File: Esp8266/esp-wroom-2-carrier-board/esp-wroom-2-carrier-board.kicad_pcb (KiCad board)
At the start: 2 copper layers, 28 parts, among them J1 DF9B-19S-1V69, J2 USB_B_Mini, Q1 MMBT2222A, Q2 MMBT2222A, U1 ESP-WROOM-02, U2 FT231XQ, U3 TPS5410DR

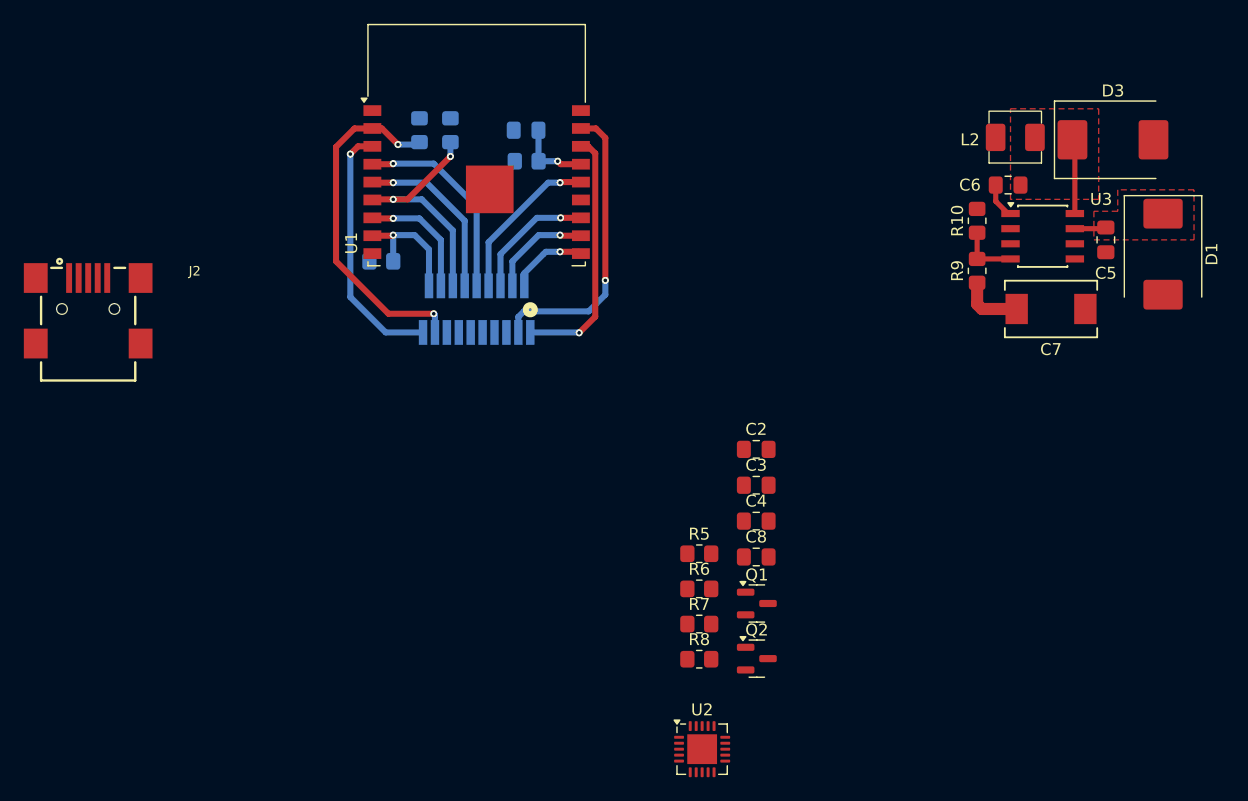
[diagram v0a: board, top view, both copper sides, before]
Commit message: Board Layout
Changed board layout to something smaller
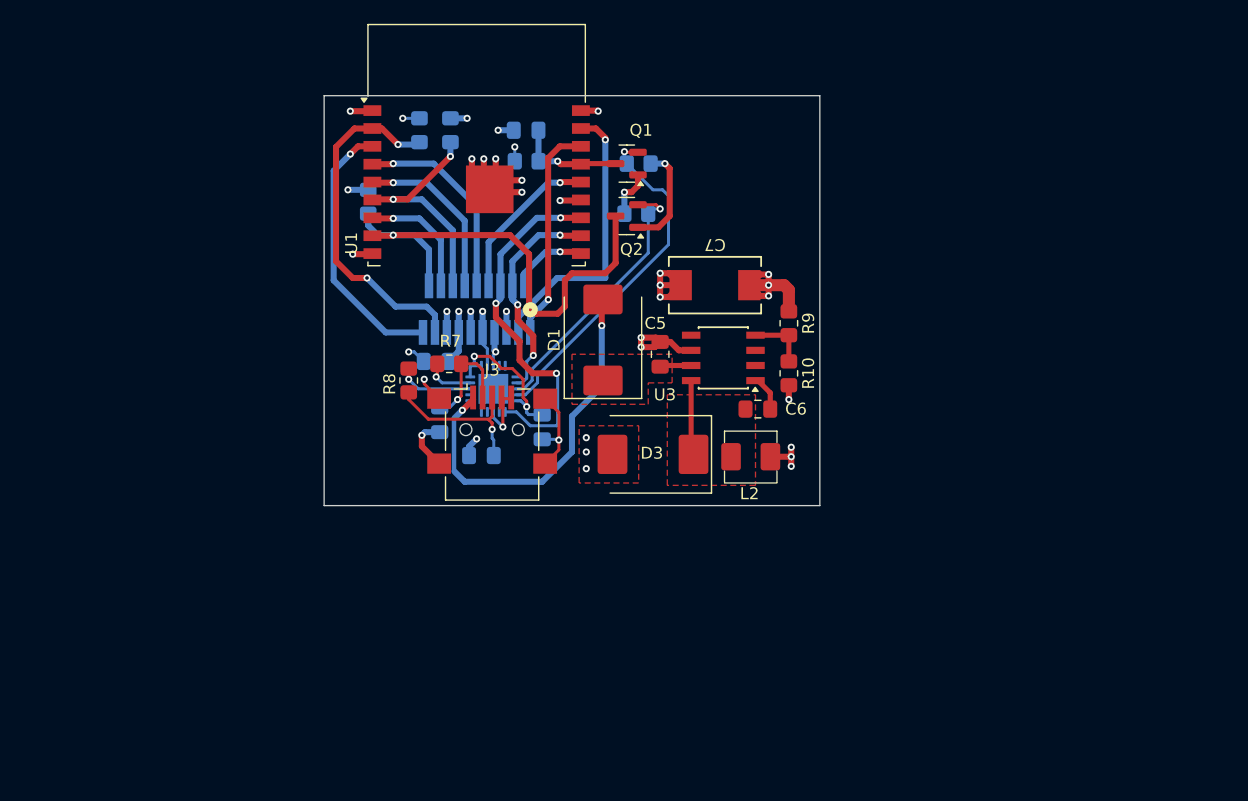
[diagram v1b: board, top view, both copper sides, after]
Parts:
- removed J2: USB_B_Mini, User_Footprint:Usb_B_mini_Wurth_65100516121
- added J3: USB_B_Mini, Connector_USB:USB_Mini-B_Lumberg_2486_01_Horizontal, F.Cu at (133.9, 101.7)
- C2, C3, C4, C8, R5, R6, U2: moved to B.Cu
- moved D1 47.5 mm to (143.2, 94.2), turned to 90 degrees
- moved D3 46.8 mm to (147.4, 103.8), turned to 180 degrees
- moved Q2 38.7 mm to (145.2, 83.8), turned to 180 degrees
- moved C5 38.6 mm to (148.0, 95.4), turned to -90 degrees
- moved Q1 38.5 mm to (145.2, 79.4), turned to 180 degrees
- moved R6 36.1 mm to (146.2, 79.4)
- moved U2 34.9 mm to (134.0, 98.3), turned to 90 degrees
- moved L2 34.8 mm to (155.6, 104.0), turned to 0 degrees
- moved R8 33.8 mm to (126.9, 97.6), turned to -90 degrees
- moved C8 31.5 mm to (129.2, 96.0), turned to 180 degrees
- moved R7 30.3 mm to (130.3, 96.2)
- moved R5 29.0 mm to (146.0, 83.6), turned to 180 degrees
- moved U3 28.7 mm to (153.3, 95.7), turned to 180 degrees
- moved C7 28.3 mm to (152.6, 89.6), turned to 180 degrees
- moved C6 28.2 mm to (156.2, 100.0), turned to 180 degrees
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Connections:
- J1 pad 11: unconnected-(J1-Pad11) -> GND
- J1 pad 13: /Microcontroller/IO13 -> +3.3V
- J1 pad 15: unconnected-(J1-Pad15) -> GND
- J1 pad 5: unconnected-(J1-Pad5) -> +3.3V
- J1 pad 7: unconnected-(J1-Pad7) -> GND
- J1 pad 9: unconnected-(J1-Pad9) -> +3.3V
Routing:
- net GND: track 0.00 -> 69.5 mm, vias 0 -> 28
- net /Microcontroller/IO0: track 10.5 -> 42.7 mm
- net /Microcontroller/Vbus: track 0.00 -> 31.9 mm, vias 0 -> 2
- net /Microcontroller/~{RTS}: track 0.00 -> 29.3 mm, vias 0 -> 1
- net +3.3V: track 5.28 -> 31.6 mm, vias 0 -> 13
- net /Microcontroller/~{DTR}: track 0.00 -> 22.8 mm, vias 0 -> 1
- net /Microcontroller/TX0: track 10.7 -> 30.8 mm, vias 1 -> 3
- net /Microcontroller/D+: track 0.00 -> 13.1 mm, vias 0 -> 1
- net Net-(U2-3V3OUT): track 0.00 -> 13.0 mm, vias 0 -> 2
- net /Microcontroller/RX0: track 8.74 -> 18.5 mm, vias 1 -> 3
- net /Microcontroller/D-: track 0.00 -> 9.33 mm, vias 0 -> 1
- net Net-(Q2-B): track 0.00 -> 8.82 mm, vias 0 -> 1
- net Net-(U2-USBDP): track 0.00 -> 6.39 mm, vias 0 -> 1
- net Net-(U2-USBDM): track 0.00 -> 4.21 mm, vias 0 -> 1
- net Net-(Q1-B): track 0.00 -> 4.07 mm, vias 0 -> 1
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- added copper zone on In2.Cu, net +3.3V
- added copper zone on F.Cu, net GND
- added copper zone on In1.Cu, net GND
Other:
- board outline added: 41.6 x 34.4 mm
- copper layers 2 -> 4

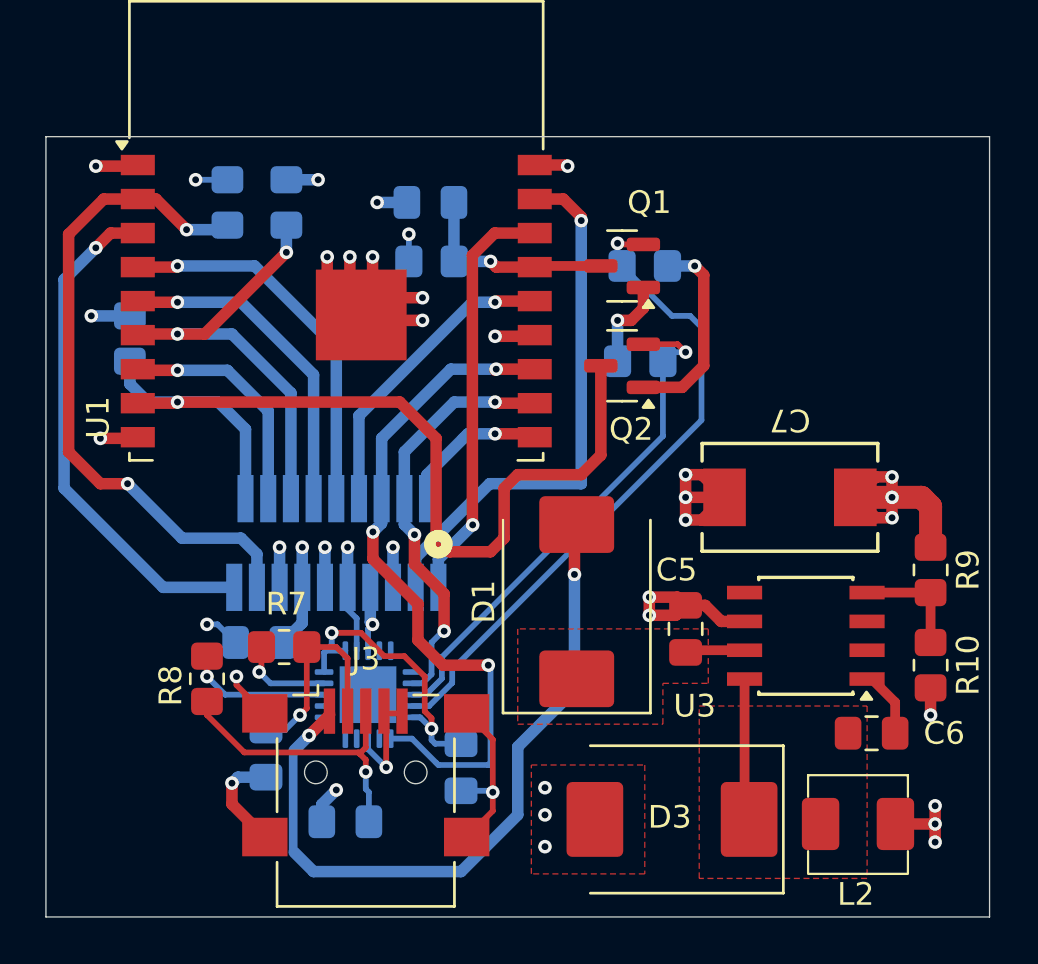
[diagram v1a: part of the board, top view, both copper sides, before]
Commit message: capacitor layout
Changed capacitor position to front layer to have enough clearance on bottom layer
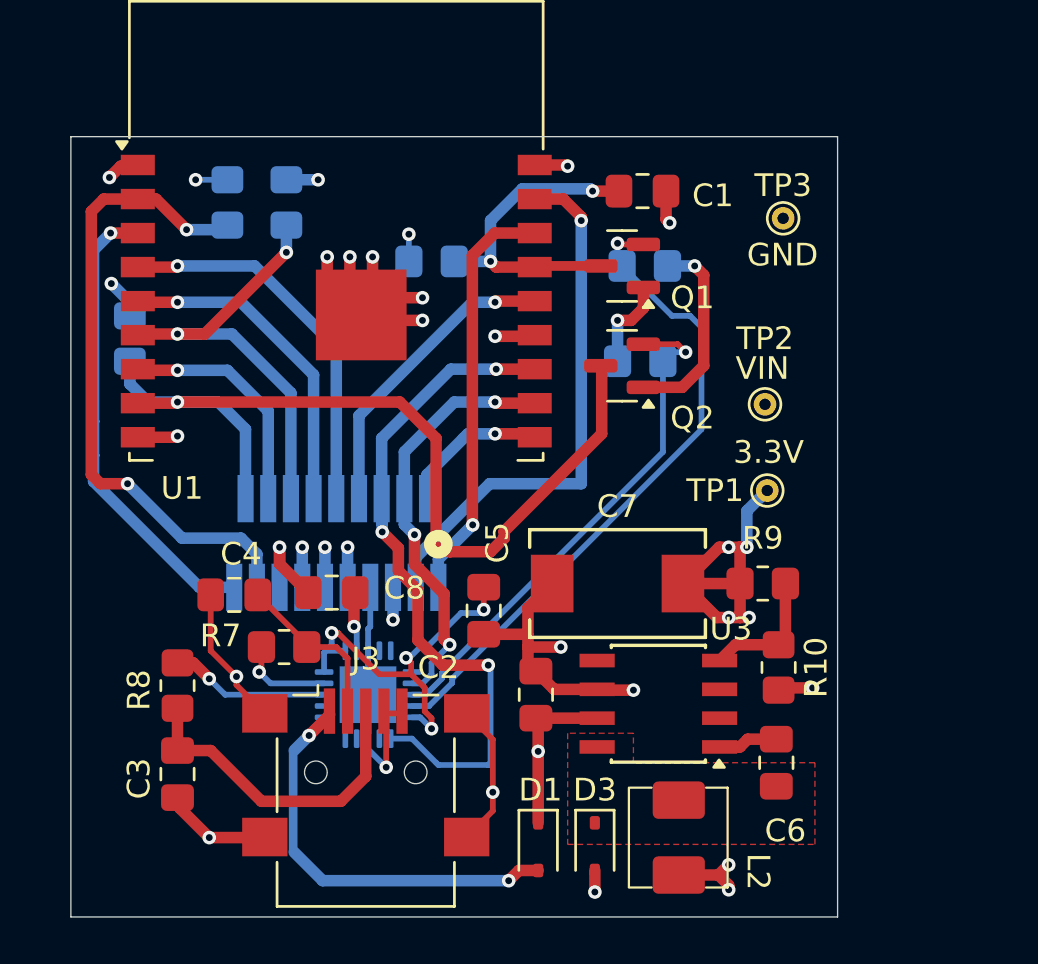
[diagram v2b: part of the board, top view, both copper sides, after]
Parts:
- added TP1: 3.3V, TestPoint:TestPoint_THTPad_D1.0mm_Drill0.5mm, F.Cu at (151.6, 89.3)
- added TP2: VIN, TestPoint:TestPoint_THTPad_D1.0mm_Drill0.5mm, F.Cu at (151.5, 85.5)
- added TP3: GND, TestPoint:TestPoint_THTPad_D1.0mm_Drill0.5mm, F.Cu at (152.3, 77.3)
- C1, C2, C3, C4, C8: moved to F.Cu
- D1: value B340 -> 1N5819ws; footprint Diode_SMD:D_SMC -> Diode_SMD:D_SOD-323
- D3: value B340 -> 1N5819WS; footprint Diode_SMD:D_SMC -> Diode_SMD:D_SOD-323
- moved D1 10.9 mm to (141.5, 105.0), turned to -90 degrees
- moved C1 9.36 mm to (146.1, 76.1), turned to 0 degrees
- moved C7 8.50 mm to (145.0, 93.4)
- moved L2 7.92 mm to (147.7, 104.6), turned to -90 degrees
- moved C3 7.69 mm to (125.6, 101.8), turned to -90 degrees
- moved R9 7.42 mm to (151.4, 93.4), turned to 0 degrees
- moved C5 7.21 mm to (141.4, 98.3)
- moved U3 7.16 mm to (146.8, 98.7)
- moved C4 7.14 mm to (128.1, 93.9), turned to 180 degrees
- moved C2 6.97 mm to (139.1, 94.6)
- moved R10 6.70 mm to (152.1, 97.1)
- moved C6 4.40 mm to (152.0, 101.3), turned to -90 degrees
- moved C8 3.88 mm to (132.4, 93.8)
- moved D3 3.61 mm to (144.0, 105.0), turned to -90 degrees
- moved R8 1.33 mm to (125.6, 97.9)
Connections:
- J1 pad 5: +3.3V -> /Microcontroller/VIN
- J1 pad 9: +3.3V -> /Microcontroller/VIN
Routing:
- net /Microcontroller/VIN: track 2.64 -> 45.3 mm, vias 0 -> 3
- net /Microcontroller/Vbus: track 31.9 -> 18.3 mm
- net /Power/PH: track 6.27 -> 0.00 mm
- net /Microcontroller/Reset: track 9.19 -> 14.7 mm, vias 1 -> 2
- net Net-(U2-3V3OUT): track 13.0 -> 16.9 mm, vias 2 -> 4
- net GND: track 69.5 -> 72.4 mm, vias 28 -> 20
- net +3.3V: track 31.6 -> 28.9 mm, vias 13 -> 12
- net /Microcontroller/IO14: track 22.6 -> 20.6 mm
- net /Microcontroller/D-: track 9.33 -> 7.63 mm, vias 1 -> 0
- net /Microcontroller/IO0: track 42.7 -> 41.1 mm
- net /Microcontroller/D+: track 13.1 -> 14.5 mm, vias 1 -> 0
- net /Microcontroller/EN: track 29.5 -> 28.7 mm
- net Net-(U3-VSENSE): track 5.00 -> 5.71 mm
- net Net-(U2-USBDP): track 6.39 -> 7.04 mm
- removed copper zone on F.Cu, net /Microcontroller/VIN
- removed copper zone on F.Cu, net GND
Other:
- board size 41.6 x 34.4 mm -> 33.8 x 34.4 mm
- board text added: "3.3V"
- board text added: "GND"
- board text added: "VIN"

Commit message: Traces
Layout traces for the PCB
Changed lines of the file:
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@@
 			(at -2.3 0 0)
 			(layer "F.SilkS")
+			(hide yes)
 			(effects
 				(font
@@
 			(size 1 1)
 			(drill 0.5)
-			(layers "F&B.Cu" "*.Mask")
+			(layers "*.Cu" "*.Mask")
 			(remove_unused_layers no)
 			(net 8 "+3.3V")
@@
 		(tags "resistor handsolder")
 		(property "Reference" "R10"
-			(at 0 -1.65 90)
+			(at -1.1 -1.65 90)
 			(layer "F.SilkS")
 			(effects
@@
 		(tags "resistor handsolder")
 		(property "Reference" "R9"
-			(at 0 -2 0)
+			(at 1.1 -1.9 0)
 			(layer "F.SilkS")
 			(effects
@@
 			(at 0 -2.9 0)
 			(layer "F.SilkS")
+			(hide yes)
 			(effects
 				(font
@@
 			(at 0 -1.448 0)
 			(layer "F.SilkS")
+			(hide yes)
 			(effects
 				(font
@@
 	)
 	(gr_text "GND"
-		(at 150.7 79.5 0)
+		(at 150.7 76 0)
 		(layer "F.SilkS")
 		(effects
@@
 		)
 	)
+	(dimension
+		(type orthogonal)
+		(layer "User.1")
+		(pts
+			(xy 132.599999 91.6) (xy 121 91.5)
+		)
+		(height -32.1)
+		(orientation 0)
+		(format
+			(prefix "")
+			(suffix "")
+			(units 3)
+			(units_format 0)
+			(precision 4)
+			(suppress_zeroes yes)
+		)
+		(style
+			(thickness 0.1)
+			(arrow_length 1.27)
+			(text_position_mode 0)
+			(arrow_direction outward)
+			(extension_height 0.58642)
+			(extension_offset 0.5)
+			(keep_text_aligned yes)
+		)
+		(gr_text "11.6"
+			(at 126.799999 58.35 0)
+			(layer "User.1")
+			(effects
+				(font
+					(size 1 1)
+					(thickness 0.15)
+				)
+			)
+		)
+	)
+	(dimension
+		(type orthogonal)
+		(layer "User.1")
+		(pts
+			(xy 132.599999 91.6) (xy 132.2 108.2)
+		)
+		(height -30.799999)
+		(orientation 1)
+		(format
+			(prefix "")
+			(suffix "")
+			(units 3)
+			(units_format 0)
+			(precision 4)
+			(suppress_zeroes yes)
+		)
+		(style
+			(thickness 0.1)
+			(arrow_length 1.27)
+			(text_position_mode 0)
+			(arrow_direction outward)
+			(extension_height 0.58642)
+			(extension_offset 0.5)
+			(keep_text_aligned yes)
+		)
+		(gr_text "16.6"
+			(at 100.65 99.9 90)
+			(layer "User.1")
+			(effects
+				(font
+					(size 1 1)
+					(thickness 0.15)
+				)
+			)
+		)
+	)
+	(dimension
+		(type orthogonal)
+		(layer "User.1")
+		(pts
+			(xy 132.599999 91.6) (xy 155 91.5)
+		)
+		(height -32.1)
+		(orientation 0)
+		(format
+			(prefix "")
+			(suffix "")
+			(units 3)
+			(units_format 0)
+			(precision 4)
+			(suppress_zeroes yes)
+		)
+		(style
+			(thickness 0.1)
+			(arrow_length 1.27)
+			(text_position_mode 0)
+			(arrow_direction outward)
+			(extension_height 0.58642)
+			(extension_offset 0.5)
+			(keep_text_aligned yes)
+		)
+		(gr_text "22.4"
+			(at 143.8 58.35 0)
+			(layer "User.1")
+			(effects
+				(font
+					(size 1 1)
+					(thickness 0.15)
+				)
+			)
+		)
+	)
+	(dimension
+		(type orthogonal)
+		(layer "User.1")
+		(pts
+			(xy 132.599999 91.6) (xy 132.7 73.7)
+		)
+		(height -30.799999)
+		(orientation 1)
+		(format
+			(prefix "")
+			(suffix "")
+			(units 3)
+			(units_format 0)
+			(precision 4)
+			(suppress_zeroes yes)
+		)
+		(style
+			(thickness 0.1)
+			(arrow_length 1.27)
+			(text_position_mode 0)
+			(arrow_direction outward)
+			(extension_height 0.58642)
+			(extension_offset 0.5)
+			(keep_text_aligned yes)
+		)
+		(gr_text "17.9"
+			(at 100.65 82.65 90)
+			(layer "User.1")
+			(effects
+				(font
+					(size 1 1)
+					(thickness 0.15)
+				)
+			)
+		)
+	)
